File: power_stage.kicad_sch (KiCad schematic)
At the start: 45 parts, among them J3 4 mm terminal, J4 4 mm terminal, Q3 FQP19N20C, Q4 FQP19N20C, Q5 FQP19N20C, Q6 FQP19N20C, U3 NCS21802, U4 NCS21802, U5 TLV9062, U6 TLV9062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

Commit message: Schematic progress.
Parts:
- added C12, C13, C14, C15: 1u, Capacitor_SMD:C_2220_5750Metric_Pad1.97x5.40mm_HandSolder, symbol Device:C
- added C29: 100n, Capacitor_SMD:C_0603_1608Metric_Pad1.08x0.95mm_HandSolder, symbol Device:C
- added J2: red_terminal, DC_load:4mm_terminal_red, symbol Connector:Screw_Terminal_01x01
- added J5: black terminal, DC_load:4mm_terminal_black, symbol Connector:Screw_Terminal_01x01
- added R29, R32: 1Meg, Resistor_SMD:R_0603_1608Metric_Pad0.98x0.95mm_HandSolder, symbol Device:R
- added R30, R33: 50k, Resistor_SMD:R_0603_1608Metric_Pad0.98x0.95mm_HandSolder, symbol Device:R
- added U13: TLV9062, symbol Amplifier_Operational:TLV9062
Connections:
- net 5V: no longer C46.2, C9.2, U3.8 (V+), U4.8 (V+)
- net GND: now also C12.2, C13.2, C14.2, C15.2, C29.1, R30.2, U13.4 (V-)
- net INPUT_POWER: now also C12.1, C13.1, C14.1, C15.1
- new net: R29.1, R30.1, U13.3 (+)
- new net: R32.1, R33.2, U13.2 (-)
- new net 3V3: C29.2, C46.2, C9.2, U13.8 (V+), U3.8 (V+), U4.8 (V+)
- new net V_SENSE: R33.1, U13.1
- new net V_SENSE+: J2.1 (Pin_1), R29.2
- new net V_SENSE-: J5.1 (Pin_1), R32.2
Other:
- moved on the sheet: C1, C10, C11, C2, C20, C3, C4, C5, C6, C7, Q3, Q4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

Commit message: aesthetics.
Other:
- moved on the sheet: C8, HS1, J2, J3, J4, J5, R29, R30, R32, R33, U13A

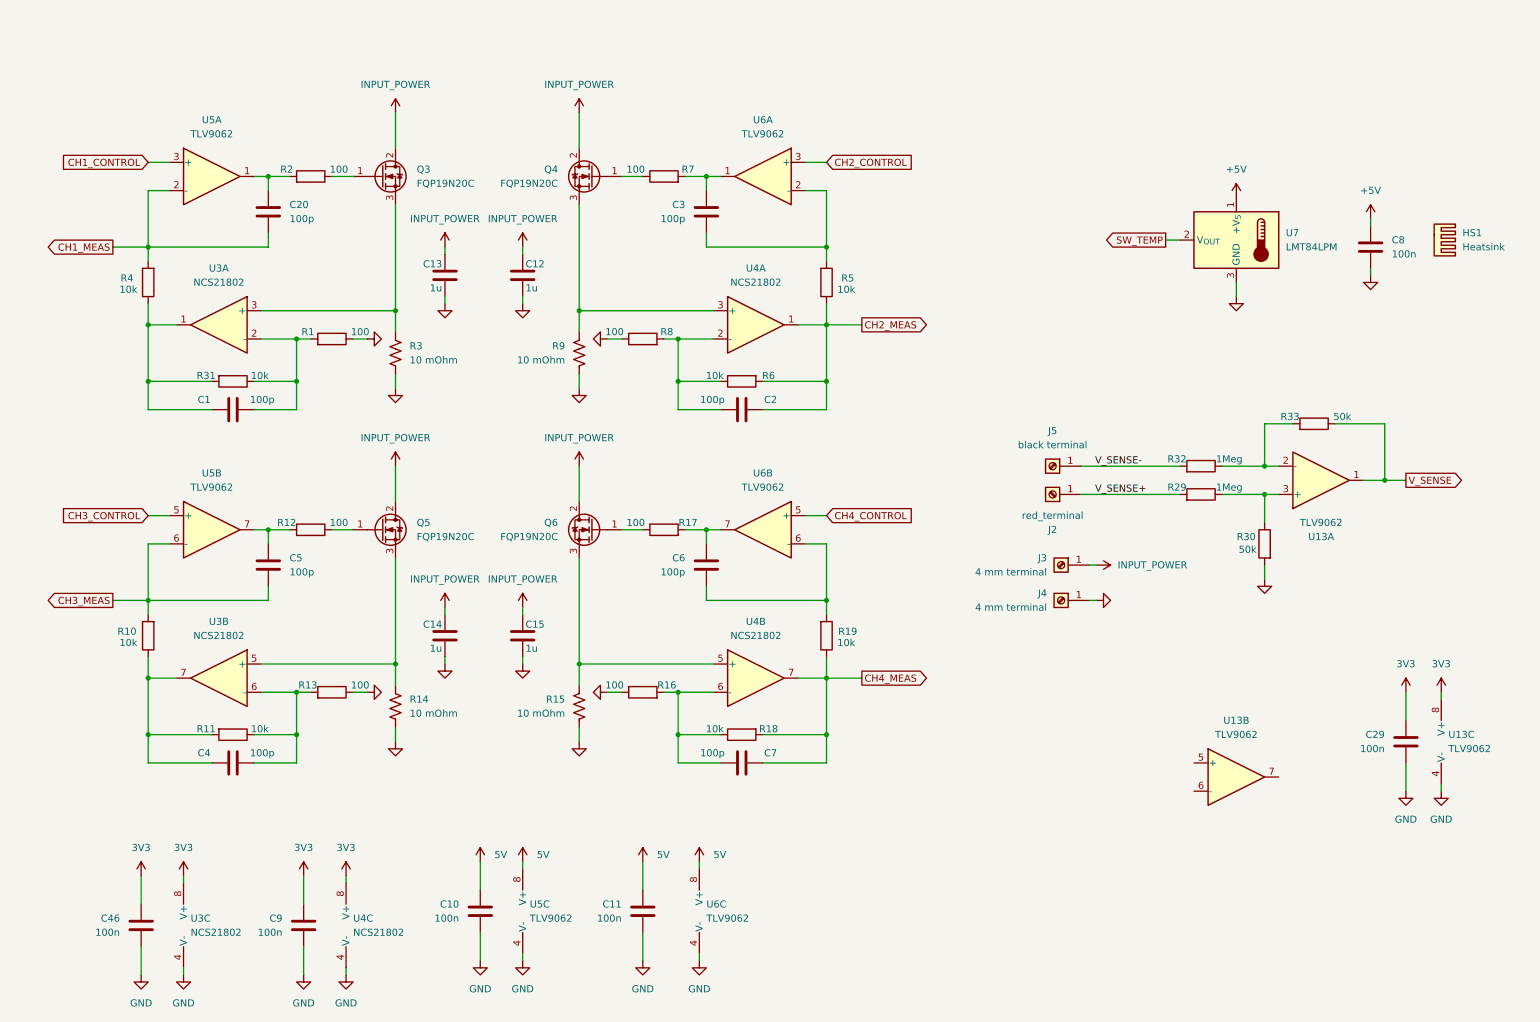
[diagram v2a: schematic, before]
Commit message: Schematic and placement update.
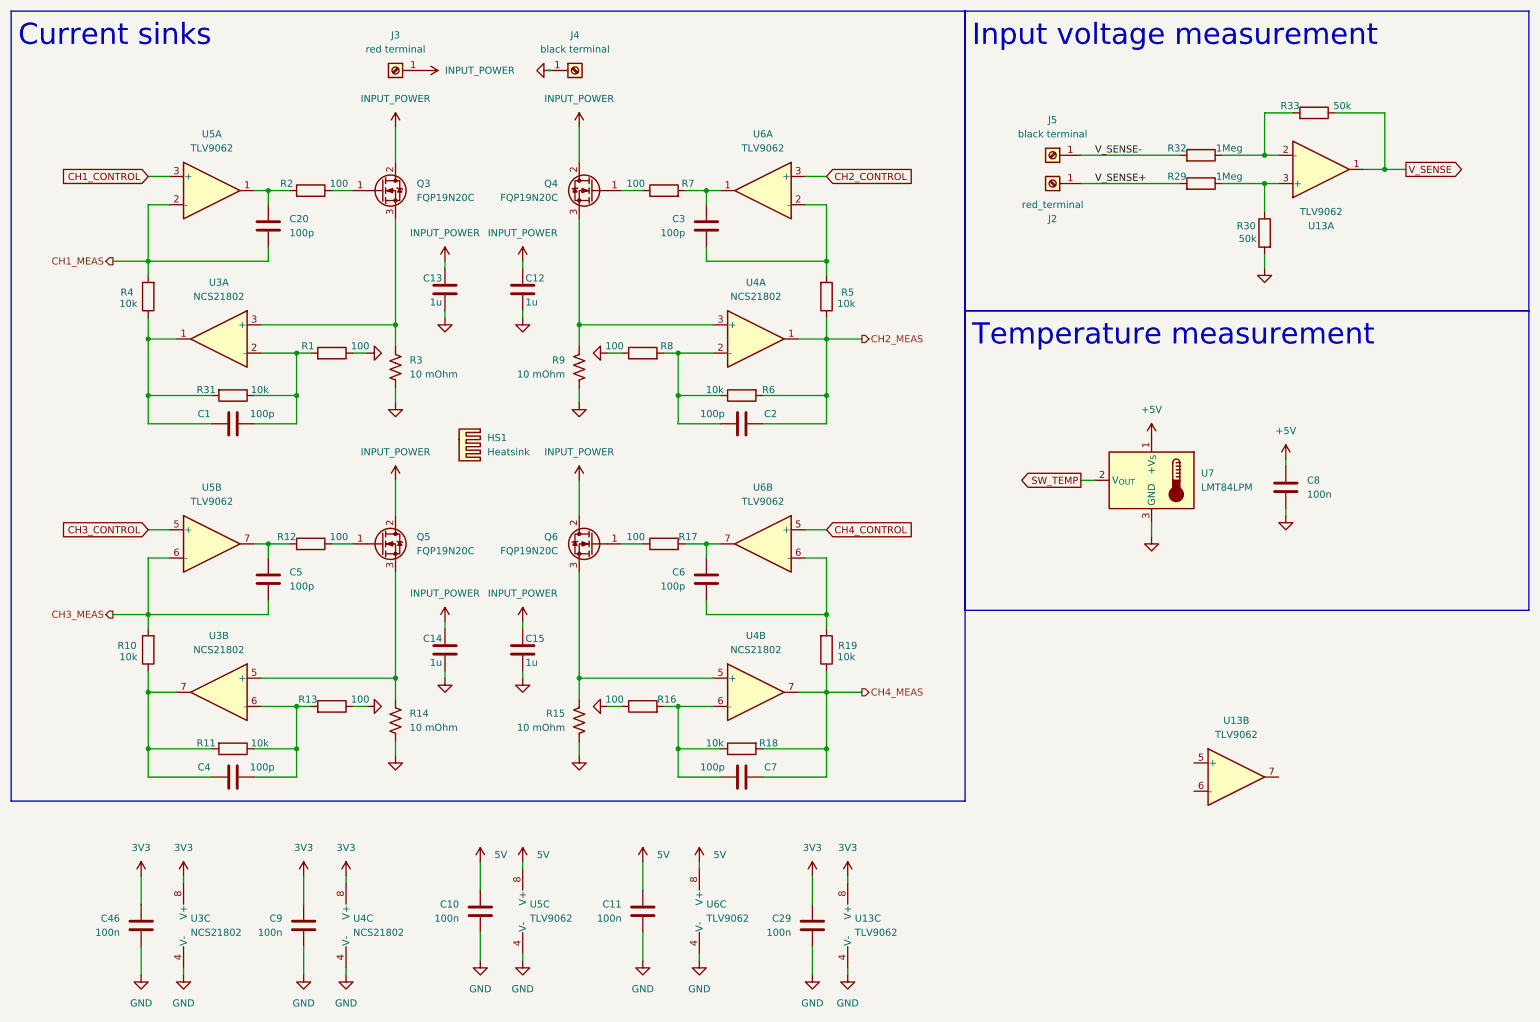
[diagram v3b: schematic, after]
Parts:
- J3: value 4 mm terminal -> red terminal
- J4: value 4 mm terminal -> black terminal
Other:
- note added: "Current sinks"
- note added: "Input voltage measurement"
- note added: "Temperature measurement"
- moved on the sheet: C1, C12, C13, C14, C15, C2, C20, C29, C3, C4, C5, C6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
